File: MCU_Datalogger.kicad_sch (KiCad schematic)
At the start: 25 parts, among them J1 Conn_01x02_Pin, U1 24LC1025, U2 24LC1025, U3 DS1337S_, U4 ATMEGA328P-AU, Y1 32.768kHz, Y2 16MHz

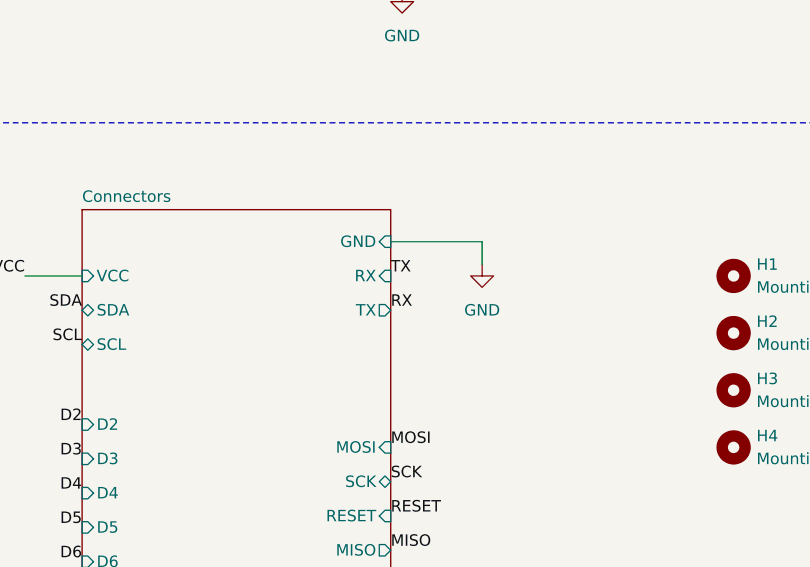
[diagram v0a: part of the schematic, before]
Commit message: Fixed RX TX misconnections
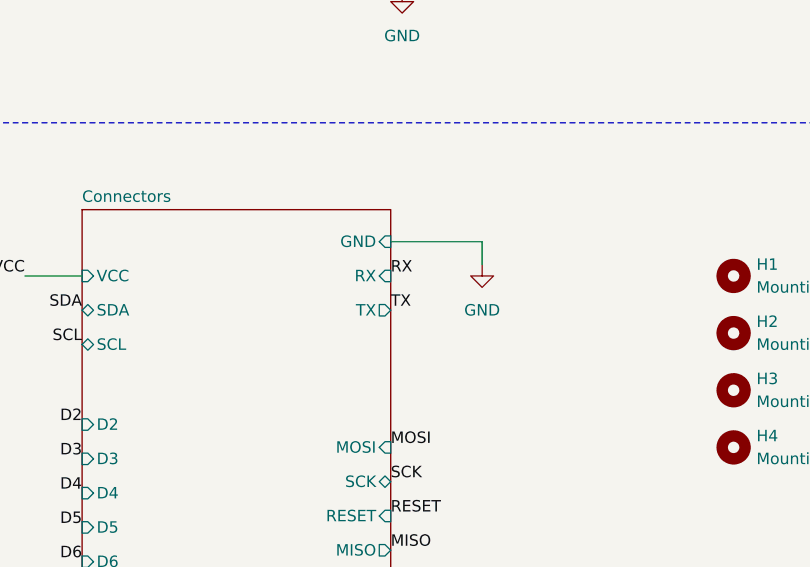
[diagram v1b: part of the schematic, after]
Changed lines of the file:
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@@
 		)
 	)
-	(label "RX"
+	(label "TX"
 		(at 228.6 121.92 0)
 		(effects
@@
 		)
 	)
-	(label "TX"
+	(label "RX"
 		(at 228.6 118.11 0)
 		(effects
